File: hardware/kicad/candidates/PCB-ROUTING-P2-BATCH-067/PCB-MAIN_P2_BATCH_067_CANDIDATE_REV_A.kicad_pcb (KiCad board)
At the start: 6 copper layers, 110 x 75 mm, 251 parts, among them J10 U.FL-R-SMT-1(60), J11 USB4105-GF-A-120, J12 MEM2052-00-195-00-A, J13 504050-0291, J6 2336582-1, J7 2336582-1, J8 U.FL-R-SMT-1(60), J9 U.FL-R-SMT-1(60), Q1 MMBT3904,215, Q2 MMBT3904,215, Q3 MMBT3904,215, Q4 Si1016X-T1-GE3, U1 STM32U585VIT6Q, U10 E22-900M22S, U11 MDBT50Q-P1MV2, U13 TS3A27518EPWR, U14 ESDALC6V1-5P6, U15 ESDALC6V1-5P6, U16 SN74AXC8T245PWR, U17 SN74LVC32APWR, U18 SN74AXC1T45DRLR, U19 TPD4E05U06DQAR, U2 W25Q512JVFIQ, U20 TPD4E05U06DQAR, U21 TPD4E05U06DQAR, U22 TPD4E05U06DQAR, U23 TPD4E05U06DQAR, U24 TPD4E05U06DQAR, U25 TPD2EUSB30DRTR, U26 TPD2EUSB30DRTR, U27 TPD4E05U06DQAR, U3 LIS2DW12TR, U4 STTS22HTR, U5 LT6000IDCB#TRMPBF, U6 SN74LVC1G07DBVR, U7 SN74AXC8T245PWR, U8 BG95-M3, U9 MAX-M10S-00B, X1 SiT1552AI-JE-DCC-32.768D

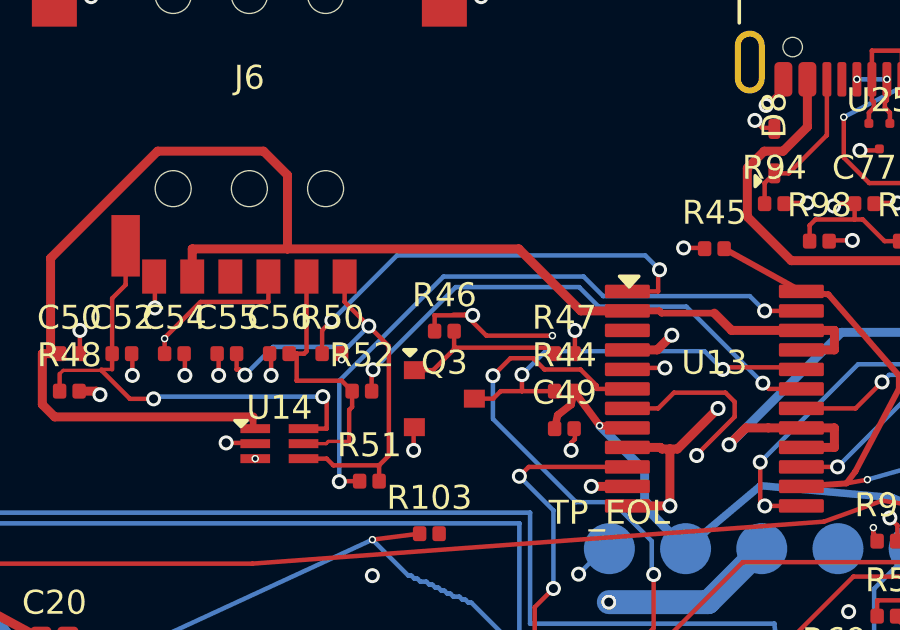
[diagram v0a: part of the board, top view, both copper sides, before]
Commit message: PCB-MAIN: snap SIM_MUX_EN branch to existing track endpoint
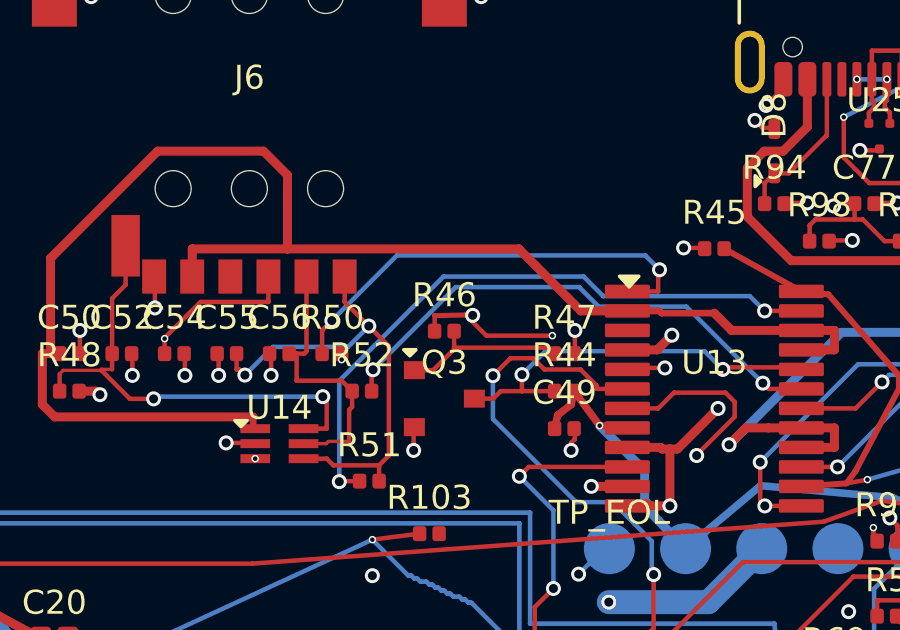
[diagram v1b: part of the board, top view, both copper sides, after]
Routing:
- net SIM_MUX_EN: track 23.9 -> 24.5 mm
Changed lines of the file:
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@@
   (segment (start 31.1 15.9) (end 28.9 15.9) (width 0.15) (layer "F.Cu") (net 156))
   (segment (start 28.9 15.9) (end 28.2 15.2) (width 0.15) (layer "F.Cu") (net 156))
-  (segment (start 28.2 15.2) (end 27.8 15.2) (width 0.15) (layer "F.Cu") (net 156))
+  (segment (start 28.2 15.2) (end 27.175 15.223) (width 0.15) (layer "F.Cu") (net 156))
   (segment (start 59.3 25.5) (end 59.1 25.5) (width 0.15) (layer "F.Cu") (net 160))
   (segment (start 59.1 25.5) (end 58.8 25.8) (width 0.15) (layer "F.Cu") (net 160))
